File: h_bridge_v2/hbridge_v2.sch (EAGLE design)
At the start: 28 parts, among them J2 1X2-3.5MM, J3 1X2-3.5MM, J4 AVR_SPI_PROG_3X2OFFSET_PADS, Q5 200mA/40V, Q6 200mA/40V, Q7 200mA/40V, Q8 200mA/40V, U1 328P

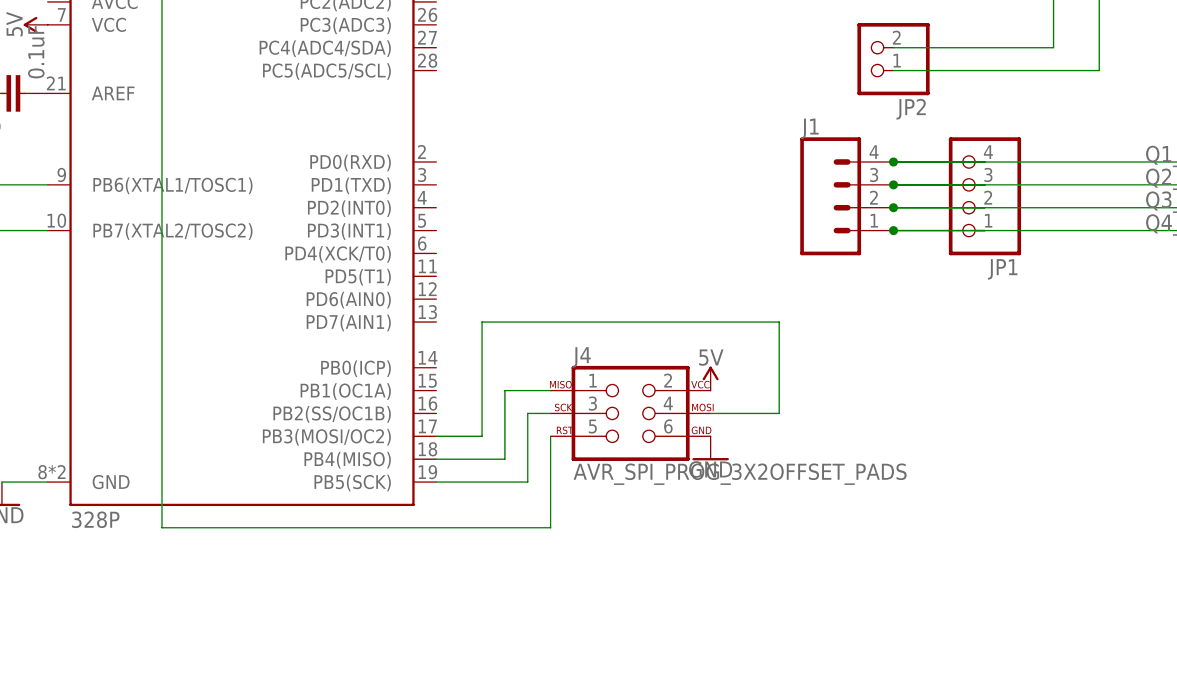
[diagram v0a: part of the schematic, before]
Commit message: added connections to PWM pins
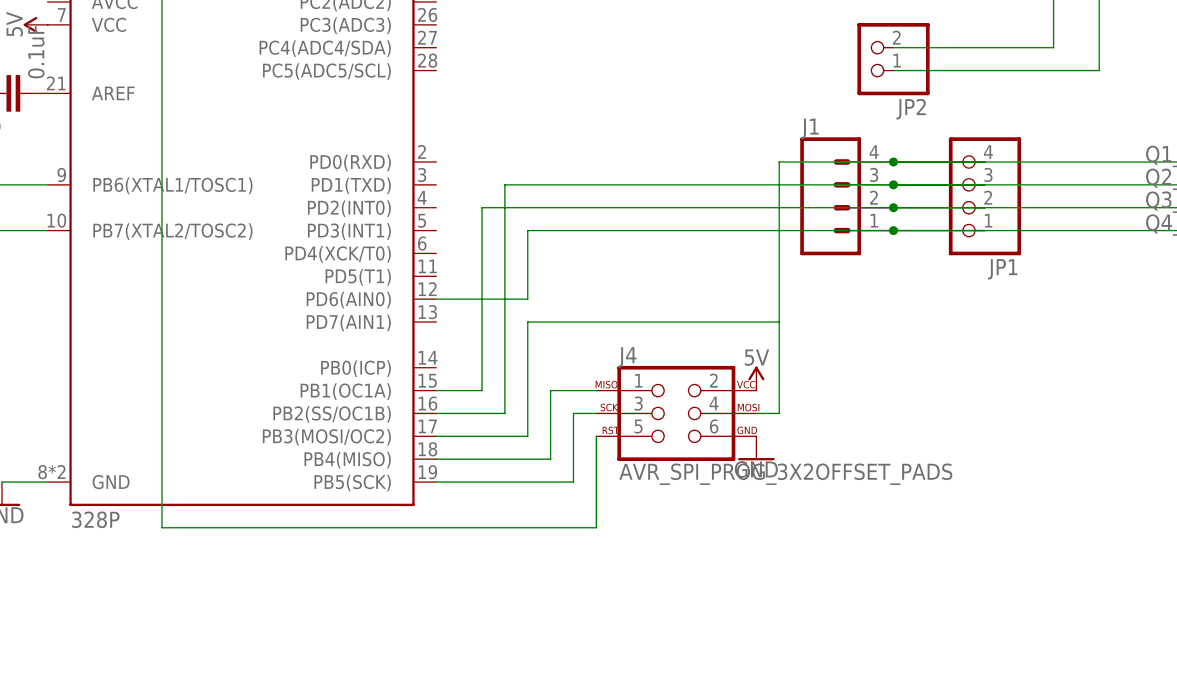
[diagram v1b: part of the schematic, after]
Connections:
- removed net N$18: J4.4, U1.PB3(MOSI/OC2)
- net Q1_INPUT: now also J4.4, U1.PB3(MOSI/OC2)
- net Q2_INPUT: now also U1.PB2(SS/OC1B)
- net Q3_INPUT: now also U1.PB1(OC1A)
- net Q4_INPUT: now also U1.PD6(AIN0)
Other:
- moved on the sheet: J4
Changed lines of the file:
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@@
 <attribute name="VALUE" x="-139.7" y="45.466" size="1.778" layer="96" align="top-center"/>
 </instance>
-<instance part="J4" gate="G$1" x="-68.58" y="12.7" smashed="yes">
-<attribute name="NAME" x="-73.66" y="18.288" size="1.778" layer="95" font="vector"/>
-<attribute name="VALUE" x="-73.66" y="5.334" size="1.778" layer="96" font="vector"/>
-</instance>
-<instance part="SUPPLY9" gate="G$1" x="-58.42" y="15.24" smashed="yes">
-<attribute name="VALUE" x="-58.42" y="18.034" size="1.778" layer="96" align="bottom-center"/>
-</instance>
-<instance part="GND11" gate="1" x="-58.42" y="7.62" smashed="yes">
-<attribute name="VALUE" x="-58.42" y="7.366" size="1.778" layer="96" align="top-center"/>
+<instance part="J4" gate="G$1" x="-63.5" y="12.7" smashed="yes">
+<attribute name="NAME" x="-68.58" y="18.288" size="1.778" layer="95" font="vector"/>
+<attribute name="VALUE" x="-68.58" y="5.334" size="1.778" layer="96" font="vector"/>
+</instance>
+<instance part="SUPPLY9" gate="G$1" x="-53.34" y="15.24" smashed="yes">
+<attribute name="VALUE" x="-53.34" y="18.034" size="1.778" layer="96" align="bottom-center"/>
+</instance>
+<instance part="GND11" gate="1" x="-53.34" y="7.62" smashed="yes">
+<attribute name="VALUE" x="-53.34" y="7.366" size="1.778" layer="96" align="top-center"/>
 </instance>
 <instance part="Y2" gate="G$1" x="-149.86" y="38.1" smashed="yes">
@@
 <junction x="-38.1" y="38.1"/>
 <wire x1="-38.1" y1="38.1" x2="-27.94" y2="38.1" width="0.1524" layer="91"/>
+<pinref part="U1" gate="U1" pin="PB2(SS/OC1B)"/>
+<wire x1="-88.9" y1="12.7" x2="-81.28" y2="12.7" width="0.1524" layer="91"/>
+<wire x1="-81.28" y1="12.7" x2="-81.28" y2="38.1" width="0.1524" layer="91"/>
+<wire x1="-81.28" y1="38.1" x2="-38.1" y2="38.1" width="0.1524" layer="91"/>
 </segment>
 </net>
@@
 <junction x="-38.1" y="40.64"/>
 <wire x1="-38.1" y1="40.64" x2="-27.94" y2="40.64" width="0.1524" layer="91"/>
+<pinref part="J4" gate="G$1" pin="4"/>
+<wire x1="-53.34" y1="12.7" x2="-50.8" y2="12.7" width="0.1524" layer="91"/>
+<wire x1="-50.8" y1="12.7" x2="-50.8" y2="22.86" width="0.1524" layer="91"/>
+<wire x1="-50.8" y1="22.86" x2="-78.74" y2="22.86" width="0.1524" layer="91"/>
+<wire x1="-78.74" y1="22.86" x2="-78.74" y2="10.16" width="0.1524" layer="91"/>
+<pinref part="U1" gate="U1" pin="PB3(MOSI/OC2)"/>
+<wire x1="-78.74" y1="10.16" x2="-88.9" y2="10.16" width="0.1524" layer="91"/>
+<wire x1="-50.8" y1="22.86" x2="-50.8" y2="40.64" width="0.1524" layer="91"/>
+<wire x1="-50.8" y1="40.64" x2="-38.1" y2="40.64" width="0.1524" layer="91"/>
 </segment>
 </net>
@@
 <junction x="-38.1" y="33.02"/>
 <wire x1="-38.1" y1="33.02" x2="-27.94" y2="33.02" width="0.1524" layer="91"/>
+<pinref part="U1" gate="U1" pin="PD6(AIN0)"/>
+<wire x1="-88.9" y1="25.4" x2="-78.74" y2="25.4" width="0.1524" layer="91"/>
+<wire x1="-78.74" y1="25.4" x2="-78.74" y2="33.02" width="0.1524" layer="91"/>
+<wire x1="-78.74" y1="33.02" x2="-38.1" y2="33.02" width="0.1524" layer="91"/>
 </segment>
 </net>
@@
 <junction x="-38.1" y="35.56"/>
 <wire x1="-38.1" y1="35.56" x2="-27.94" y2="35.56" width="0.1524" layer="91"/>
+<pinref part="U1" gate="U1" pin="PB1(OC1A)"/>
+<wire x1="-88.9" y1="15.24" x2="-83.82" y2="15.24" width="0.1524" layer="91"/>
+<wire x1="-83.82" y1="15.24" x2="-83.82" y2="35.56" width="0.1524" layer="91"/>
+<wire x1="-83.82" y1="35.56" x2="-38.1" y2="35.56" width="0.1524" layer="91"/>
 </segment>
 </net>
@@
 <pinref part="S1" gate="G$1" pin="2"/>
 <pinref part="J4" gate="G$1" pin="5"/>
-<wire x1="-76.2" y1="10.16" x2="-76.2" y2="0" width="0.1524" layer="91"/>
-<wire x1="-76.2" y1="0" x2="-119.38" y2="0" width="0.1524" layer="91"/>
+<wire x1="-71.12" y1="10.16" x2="-71.12" y2="0" width="0.1524" layer="91"/>
+<wire x1="-71.12" y1="0" x2="-119.38" y2="0" width="0.1524" layer="91"/>
 <wire x1="-119.38" y1="0" x2="-119.38" y2="71.12" width="0.1524" layer="91"/>
 <wire x1="-119.38" y1="71.12" x2="-134.62" y2="71.12" width="0.1524" layer="91"/>
@@
 <segment>
 <pinref part="U1" gate="U1" pin="PB4(MISO)"/>
-<wire x1="-88.9" y1="7.62" x2="-81.28" y2="7.62" width="0.1524" layer="91"/>
-<wire x1="-81.28" y1="7.62" x2="-81.28" y2="15.24" width="0.1524" layer="91"/>
+<wire x1="-88.9" y1="7.62" x2="-76.2" y2="7.62" width="0.1524" layer="91"/>
+<wire x1="-76.2" y1="7.62" x2="-76.2" y2="15.24" width="0.1524" layer="91"/>
 <pinref part="J4" gate="G$1" pin="1"/>
-<wire x1="-81.28" y1="15.24" x2="-76.2" y2="15.24" width="0.1524" layer="91"/>
+<wire x1="-76.2" y1="15.24" x2="-71.12" y2="15.24" width="0.1524" layer="91"/>
 </segment>
 </net>
@@
 <segment>
 <pinref part="U1" gate="U1" pin="PB5(SCK)"/>
-<wire x1="-88.9" y1="5.08" x2="-78.74" y2="5.08" width="0.1524" layer="91"/>
-<wire x1="-78.74" y1="5.08" x2="-78.74" y2="12.7" width="0.1524" layer="91"/>
+<wire x1="-88.9" y1="5.08" x2="-73.66" y2="5.08" width="0.1524" layer="91"/>
+<wire x1="-73.66" y1="5.08" x2="-73.66" y2="12.7" width="0.1524" layer="91"/>
 <pinref part="J4" gate="G$1" pin="3"/>
-<wire x1="-78.74" y1="12.7" x2="-76.2" y2="12.7" width="0.1524" layer="91"/>
-</segment>
-</net>
-<net name="N$18" class="0">
-<segment>
-<pinref part="J4" gate="G$1" pin="4"/>
-<wire x1="-58.42" y1="12.7" x2="-50.8" y2="12.7" width="0.1524" layer="91"/>
-<wire x1="-50.8" y1="12.7" x2="-50.8" y2="22.86" width="0.1524" layer="91"/>
-<wire x1="-50.8" y1="22.86" x2="-83.82" y2="22.86" width="0.1524" layer="91"/>
-<wire x1="-83.82" y1="22.86" x2="-83.82" y2="10.16" width="0.1524" layer="91"/>
-<pinref part="U1" gate="U1" pin="PB3(MOSI/OC2)"/>
-<wire x1="-83.82" y1="10.16" x2="-88.9" y2="10.16" width="0.1524" layer="91"/>
-</segment>
-</net>
+<wire x1="-73.66" y1="12.7" x2="-71.12" y2="12.7" width="0.1524" layer="91"/>
+</segment>
+</net>

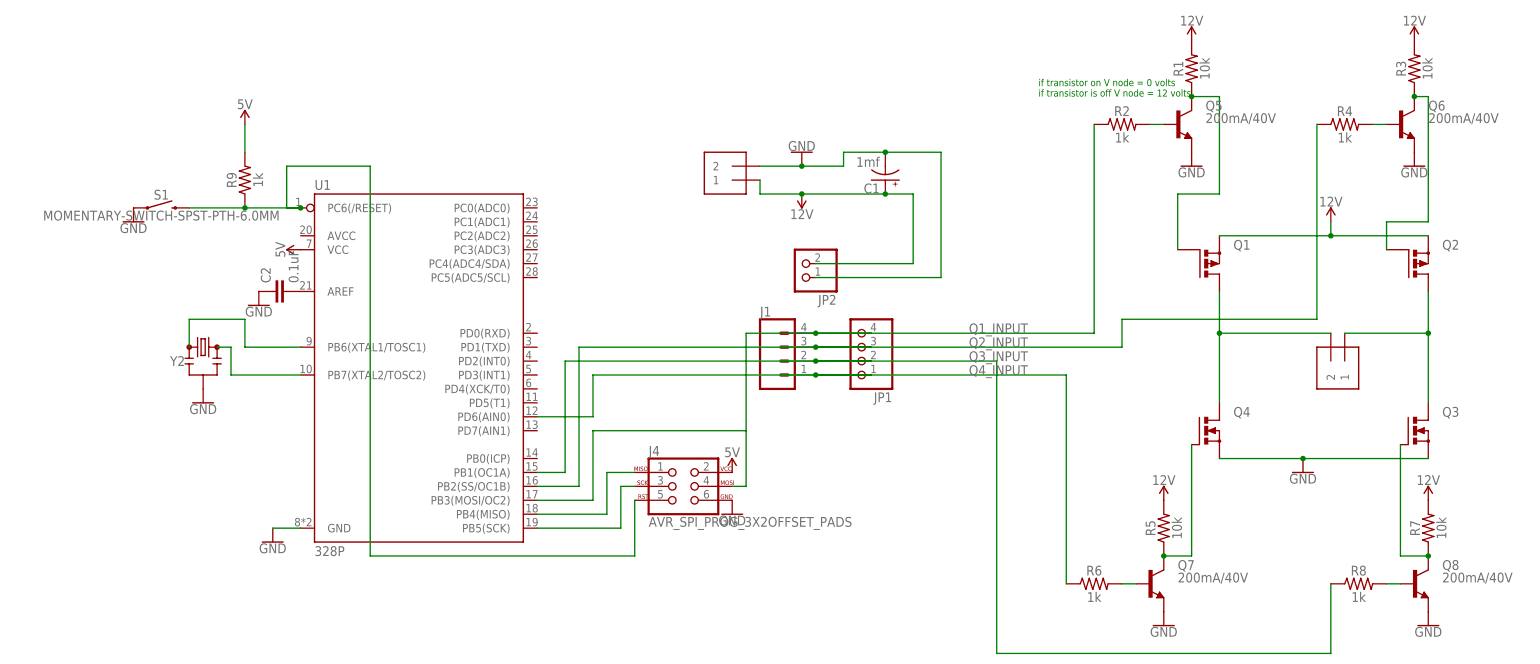
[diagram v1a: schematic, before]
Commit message: added I2C port and some topnames
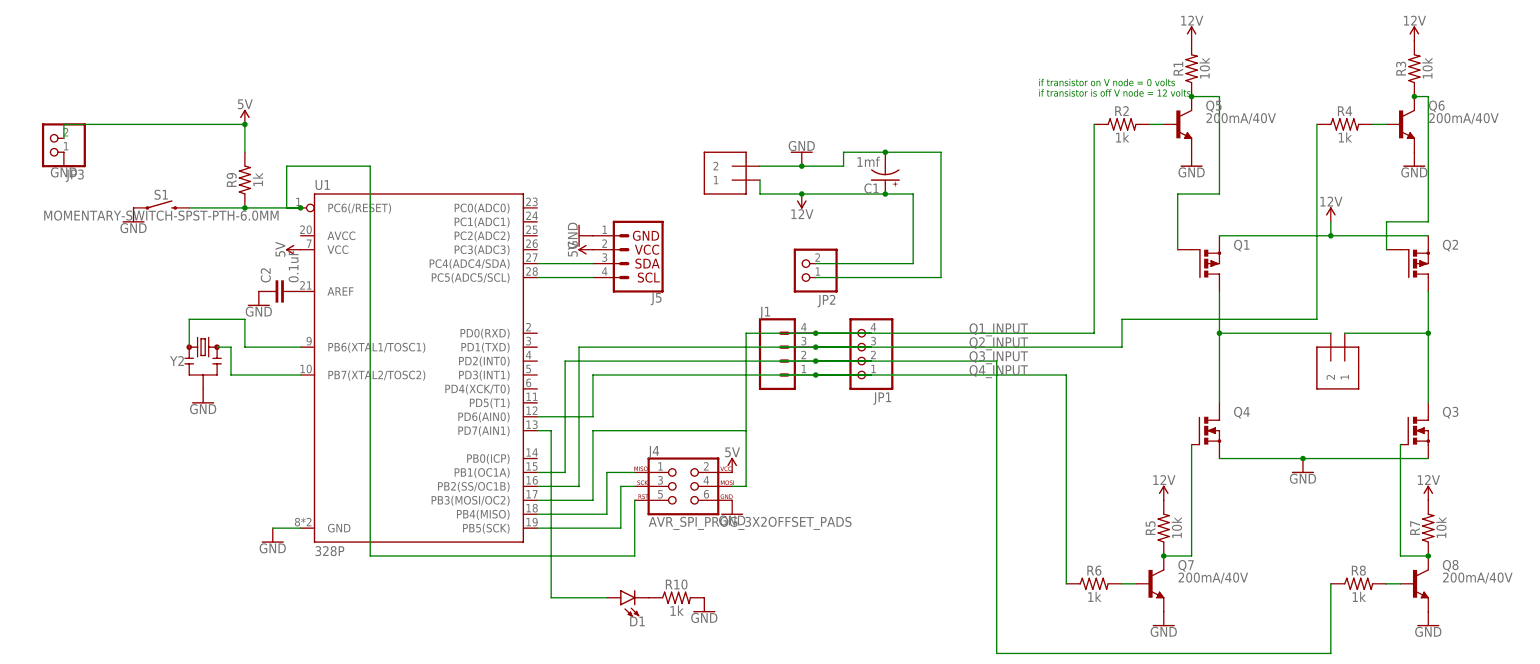
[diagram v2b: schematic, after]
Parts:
- added D1: (no value), SparkFun-LED:LED3MM
- added J5: (no value), SparkFun-Connectors:I2C_STANDARD
- added JP3: (no value), DC_LOAD_AU:PINHD-1X2
- added R10: 1k, SparkFun-Resistors:1KOHM-HORIZ-1/4W-5%
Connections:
- new net N$17: D1.A, U1.PD7(AIN1)
- new net N$18: D1.C, R10.1
- new net N$19: J5.3, U1.PC4(ADC4/SDA)
- new net N$20: J5.4, U1.PC5(ADC5/SCL)
- net 5V: now also J5.2, JP3.2
- net GND: now also J5.1, JP3.1, R10.2
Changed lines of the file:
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@@
 <part name="GND11" library="SparkFun-PowerSymbols" library_urn="urn:adsk.eagle:library:530" deviceset="GND" device=""/>
 <part name="Y2" library="SparkFun-Clocks" library_urn="urn:adsk.eagle:library:511" deviceset="RESONATOR" device="PTH-7.6X3.8" package3d_urn="urn:adsk.eagle:package:37527/1"/>
+<part name="D1" library="SparkFun-LED" library_urn="urn:adsk.eagle:library:529" deviceset="LED" device="3MM" package3d_urn="urn:adsk.eagle:package:39361/1"/>
+<part name="R10" library="SparkFun-Resistors" library_urn="urn:adsk.eagle:library:532" deviceset="1KOHM" device="-HORIZ-1/4W-5%" package3d_urn="urn:adsk.eagle:package:39658/1" value="1k"/>
+<part name="GND12" library="SparkFun-PowerSymbols" library_urn="urn:adsk.eagle:library:530" deviceset="GND" device=""/>
+<part name="JP3" library="DC_LOAD_AU" library_urn="urn:adsk.eagle:library:220454" deviceset="PINHD-1X2" device="" package3d_urn="urn:adsk.eagle:package:220539/2"/>
+<part name="GND13" library="SparkFun-PowerSymbols" library_urn="urn:adsk.eagle:library:530" deviceset="GND" device=""/>
+<part name="J5" library="SparkFun-Connectors" library_urn="urn:adsk.eagle:library:513" deviceset="I2C_STANDARD" device="" package3d_urn="urn:adsk.eagle:package:38085/1"/>
+<part name="SUPPLY10" library="SparkFun-PowerSymbols" deviceset="5V" device=""/>
+<part name="GND14" library="SparkFun-PowerSymbols" library_urn="urn:adsk.eagle:library:530" deviceset="GND" device=""/>
 </parts>
 <sheets>
@@
 <attribute name="NAME" x="-153.162" y="35.56" size="1.778" layer="95" font="vector" align="center-right"/>
 <attribute name="VALUE" x="-149.86" y="40.132" size="1.778" layer="96" font="vector" align="bottom-center"/>
+</instance>
+<instance part="D1" gate="G$1" x="-73.66" y="-7.62" smashed="yes" rot="R90">
+<attribute name="NAME" x="-69.088" y="-11.049" size="1.778" layer="95" font="vector" rot="R180"/>
+<attribute name="VALUE" x="-69.088" y="-5.715" size="1.778" layer="96" font="vector" rot="R180" align="top-left"/>
+</instance>
+<instance part="R10" gate="G$1" x="-63.5" y="-7.62" smashed="yes">
+<attribute name="NAME" x="-63.5" y="-6.096" size="1.778" layer="95" font="vector" align="bottom-center"/>
+<attribute name="VALUE" x="-63.5" y="-9.144" size="1.778" layer="96" font="vector" align="top-center"/>
+</instance>
+<instance part="GND12" gate="1" x="-58.42" y="-10.16" smashed="yes">
+<attribute name="VALUE" x="-58.42" y="-10.414" size="1.778" layer="96" align="top-center"/>
+</instance>
+<instance part="JP3" gate="G$1" x="-177.8" y="76.2" smashed="yes" rot="R180">
+<attribute name="NAME" x="-171.45" y="70.485" size="1.778" layer="95" rot="R180"/>
+<attribute name="VALUE" x="-171.45" y="81.28" size="1.778" layer="96" rot="R180"/>
+</instance>
+<instance part="GND13" gate="1" x="-175.26" y="71.12" smashed="yes">
+<attribute name="VALUE" x="-175.26" y="70.866" size="1.778" layer="96" align="top-center"/>
+</instance>
+<instance part="J5" gate="G$1" x="-71.12" y="55.88" smashed="yes" rot="R180">
+<attribute name="VALUE" x="-66.04" y="61.214" size="1.778" layer="96" font="vector" rot="R180" align="top-left"/>
+<attribute name="NAME" x="-66.04" y="48.006" size="1.778" layer="95" font="vector" rot="R180"/>
+</instance>
+<instance part="SUPPLY10" gate="G$1" x="-78.74" y="55.88" smashed="yes" rot="R90">
+<attribute name="VALUE" x="-81.534" y="55.88" size="1.778" layer="96" rot="R90" align="bottom-center"/>
+</instance>
+<instance part="GND14" gate="1" x="-81.28" y="58.42" smashed="yes" rot="R270">
+<attribute name="VALUE" x="-81.534" y="58.42" size="1.778" layer="96" rot="R270" align="top-center"/>
 </instance>
 </instances>
@@
 <pinref part="GND7" gate="1" pin="GND"/>
 <pinref part="Y2" gate="G$1" pin="2"/>
+</segment>
+<segment>
+<pinref part="R10" gate="G$1" pin="2"/>
+<pinref part="GND12" gate="1" pin="GND"/>
+</segment>
+<segment>
+<pinref part="JP3" gate="G$1" pin="1"/>
+<pinref part="GND13" gate="1" pin="GND"/>
+</segment>
+<segment>
+<pinref part="J5" gate="G$1" pin="1"/>
+<pinref part="GND14" gate="1" pin="GND"/>
 </segment>
 </net>
@@
 <pinref part="R9" gate="G$1" pin="2"/>
 <wire x1="-142.24" y1="78.74" x2="-142.24" y2="73.66" width="0.1524" layer="91"/>
+<pinref part="JP3" gate="G$1" pin="2"/>
+<wire x1="-175.26" y1="76.2" x2="-175.26" y2="78.74" width="0.1524" layer="91"/>
+<wire x1="-175.26" y1="78.74" x2="-142.24" y2="78.74" width="0.1524" layer="91"/>
+<junction x="-142.24" y="78.74"/>
 </segment>
 <segment>
@@
 <pinref part="J4" gate="G$1" pin="2"/>
 <pinref part="SUPPLY9" gate="G$1" pin="5V"/>
+</segment>
+<segment>
+<pinref part="J5" gate="G$1" pin="2"/>
+<pinref part="SUPPLY10" gate="G$1" pin="5V"/>
 </segment>
 </net>
@@
 </segment>
 </net>
+<net name="N$17" class="0">
+<segment>
+<pinref part="U1" gate="U1" pin="PD7(AIN1)"/>
+<wire x1="-88.9" y1="22.86" x2="-86.36" y2="22.86" width="0.1524" layer="91"/>
+<wire x1="-86.36" y1="22.86" x2="-86.36" y2="-7.62" width="0.1524" layer="91"/>
+<pinref part="D1" gate="G$1" pin="A"/>
+<wire x1="-86.36" y1="-7.62" x2="-76.2" y2="-7.62" width="0.1524" layer="91"/>
+</segment>
+</net>
+<net name="N$18" class="0">
+<segment>
+<pinref part="D1" gate="G$1" pin="C"/>
+<pinref part="R10" gate="G$1" pin="1"/>
+</segment>
+</net>
+<net name="N$19" class="0">
+<segment>
+<pinref part="U1" gate="U1" pin="PC4(ADC4/SDA)"/>
+<pinref part="J5" gate="G$1" pin="3"/>
+<wire x1="-88.9" y1="53.34" x2="-78.74" y2="53.34" width="0.1524" layer="91"/>
+</segment>
+</net>
+<net name="N$20" class="0">
+<segment>
+<pinref part="U1" gate="U1" pin="PC5(ADC5/SCL)"/>
+<pinref part="J5" gate="G$1" pin="4"/>
+<wire x1="-88.9" y1="50.8" x2="-78.74" y2="50.8" width="0.1524" layer="91"/>
+</segment>
+</net>
